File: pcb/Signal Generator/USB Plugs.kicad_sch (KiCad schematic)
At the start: 21 parts, among them U1 FT230XQ

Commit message: Updated pcb
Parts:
- removed C2: 10nF, symbol Device:C
- removed D3, D4: D_Schottky, symbol Device:D_Schottky
- removed FB2: 220R, symbol Device:FerriteBead
- removed R3, R4: 5.1kR, symbol Device:R
- removed USB2: UART USB, Skyward library:USB4105-GF-A, symbol Connector:USB_C_Receptacle_USB2.0
- renumbered U1 to U2, USB1 to USB
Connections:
- net 5V_USB1 is gone; now on net 5V_USB: FB1.2
- net USB1_D+ is gone; now on net USB_D+: USB.A6 (D+), USB.B6 (D+)
- net USB1_D- is gone; now on net USB_D-: USB.A7 (D-), USB.B7 (D-)
- net USB_D-: now reaches C4.1, R5.1
- net USB_D+: now reaches C3.1, R6.2
- no-connect marks 8 -> 6
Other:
- note added: "USB Plug"
- note removed: "Double power source"
- note removed: "USB Plugs"
- moved on the sheet: C1, FB1, R1, R2, USB

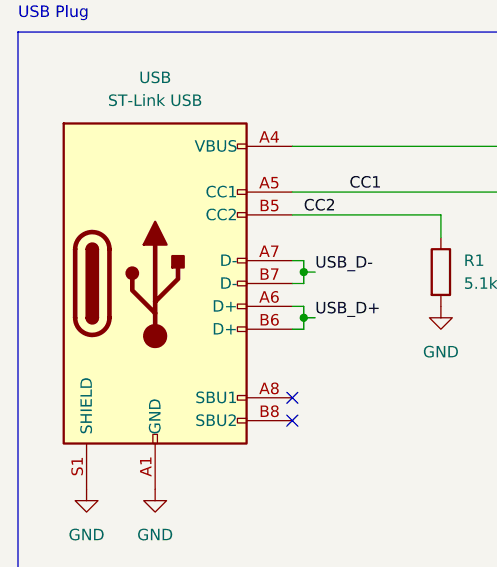
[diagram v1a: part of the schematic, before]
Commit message: Updated schematic with almost final front end
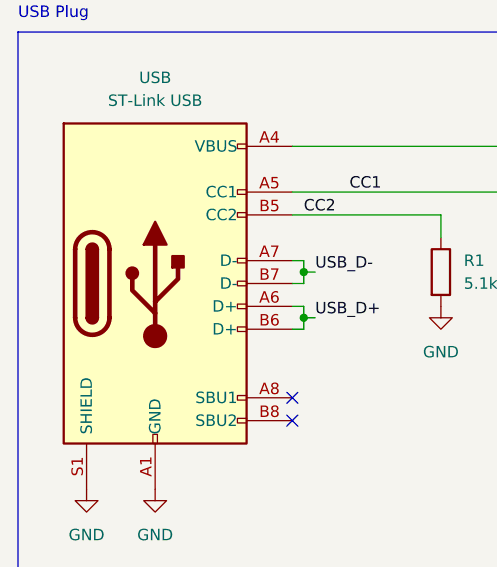
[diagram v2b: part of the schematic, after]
